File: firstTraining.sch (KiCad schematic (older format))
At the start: 5 parts

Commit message: 配線した
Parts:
- added C?: CP1, symbol Device:CP1
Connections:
- net AC: now reaches T?.1 (AA)
- net GND: now reaches T?.2 (AB)
- net GND: now also C?.2, C?.2, T?.4 (SC), U?.2 (GND), C?.2
- net at T?.3 (SA): now also D?.4 (~~)
- net at T?.5 (SB): now also D?.3 (~~)
- net at D?.1 (+): now also C?.1, U?.1 (IN)
- net at D?.2 (-): now also C?.1
- net at U?.3 (OUT): now also C?.1
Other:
- moved on the sheet: C?, D?, T?, U?
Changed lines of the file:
@@
 EESchema Schematic File Version 4
+LIBS:firstTraining-cache
 EELAYER 26 0
 EELAYER END
@@
 L Device:Transformer_1P_SS T?
 U 1 1 5BD5E741
-P 3900 2550
-F 0 "T?" H 3900 2928 50  0000 C CNN
-F 1 "Transformer_1P_SS" H 3900 2837 50  0000 C CNN
-F 2 "" H 3900 2550 50  0001 C CNN
-F 3 "~" H 3900 2550 50  0001 C CNN
-	1    3900 2550
+P 1700 1500
+F 0 "T?" H 1700 1878 50  0000 C CNN
+F 1 "Transformer_1P_SS" H 1700 1787 50  0000 C CNN
+F 2 "" H 1700 1500 50  0001 C CNN
+F 3 "~" H 1700 1500 50  0001 C CNN
+	1    1700 1500
 	1    0    0    -1
 $EndComp
@@
 L Device:D_Bridge_+-AA D?
 U 1 1 5BD5E940
-P 5000 2550
-F 0 "D?" H 5341 2596 50  0000 L CNN
-F 1 "D_Bridge_+-AA" H 5341 2505 50  0000 L CNN
-F 2 "" H 5000 2550 50  0001 C CNN
-F 3 "~" H 5000 2550 50  0001 C CNN
-	1    5000 2550
+P 2800 1500
+F 0 "D?" H 3141 1546 50  0000 L CNN
+F 1 "D_Bridge_+-AA" H 3141 1455 50  0000 L CNN
+F 2 "" H 2800 1500 50  0001 C CNN
+F 3 "~" H 2800 1500 50  0001 C CNN
+	1    2800 1500
 	1    0    0    -1
 $EndComp
@@
 L Device:CP1 C?
 U 1 1 5BD5EB54
-P 6300 2550
-F 0 "C?" H 6415 2596 50  0000 L CNN
-F 1 "CP1" H 6415 2505 50  0000 L CNN
-F 2 "" H 6300 2550 50  0001 C CNN
-F 3 "~" H 6300 2550 50  0001 C CNN
-	1    6300 2550
+P 4100 1500
+F 0 "C?" H 4215 1546 50  0000 L CNN
+F 1 "CP1" H 4215 1455 50  0000 L CNN
+F 2 "" H 4100 1500 50  0001 C CNN
+F 3 "~" H 4100 1500 50  0001 C CNN
+	1    4100 1500
 	1    0    0    -1
 $EndComp
@@
 L Regulator_Linear:L7805 U?
 U 1 1 5BD5FA9A
-P 7200 2500
-F 0 "U?" H 7200 2742 50  0000 C CNN
-F 1 "L7805" H 7200 2651 50  0000 C CNN
-F 2 "" H 7225 2350 50  0001 L CIN
-F 3 "http://www.st.com/content/ccc/resource/technical/document/datasheet/41/4f/b3/b0/12/d4/47/88/CD00000444.pdf/files/CD00000444.pdf/jcr:content/translations/en.CD00000444.pdf" H 7200 2450 50  0001 C CNN
-	1    7200 2500
+P 5000 1450
+F 0 "U?" H 5000 1692 50  0000 C CNN
+F 1 "L7805" H 5000 1601 50  0000 C CNN
+F 2 "" H 5025 1300 50  0001 L CIN
+F 3 "http://www.st.com/content/ccc/resource/technical/document/datasheet/41/4f/b3/b0/12/d4/47/88/CD00000444.pdf/files/CD00000444.pdf/jcr:content/translations/en.CD00000444.pdf" H 5000 1400 50  0001 C CNN
+	1    5000 1450
 	1    0    0    -1
 $EndComp
@@
 L Device:C C?
 U 1 1 5BD5FBB0
-P 7900 2600
-F 0 "C?" H 8015 2646 50  0000 L CNN
-F 1 "C" H 8015 2555 50  0000 L CNN
-F 2 "" H 7938 2450 50  0001 C CNN
-F 3 "~" H 7900 2600 50  0001 C CNN
-	1    7900 2600
+P 5700 1550
+F 0 "C?" H 5815 1596 50  0000 L CNN
+F 1 "C" H 5815 1505 50  0000 L CNN
+F 2 "" H 5738 1400 50  0001 C CNN
+F 3 "~" H 5700 1550 50  0001 C CNN
+	1    5700 1550
 	1    0    0    -1
 $EndComp
+$Comp
+L power:AC #PWR?
+U 1 1 5BD65D78
+P 1050 1300
+F 0 "#PWR?" H 1050 1200 50  0001 C CNN
+F 1 "AC" H 1050 1575 50  0000 C CNN
+F 2 "" H 1050 1300 50  0001 C CNN
+F 3 "" H 1050 1300 50  0001 C CNN
+	1    1050 1300
+	1    0    0    -1
+$EndComp
+Wire Wire Line
+	2100 1300 2350 1300
+Wire Wire Line
+	2350 1300 2350 1200
+Wire Wire Line
+	2350 1200 2800 1200
+Wire Wire Line
+	2400 1700 2400 1800
+Wire Wire Line
+	2400 1800 2800 1800
+Wire Wire Line
+	2100 1700 2400 1700
+Wire Wire Line
+	1050 1300 1300 1300
+$Comp
+L power:GND #PWR?
+U 1 1 5BD65E35
+P 1000 1700
+F 0 "#PWR?" H 1000 1450 50  0001 C CNN
+F 1 "GND" H 1005 1527 50  0000 C CNN
+F 2 "" H 1000 1700 50  0001 C CNN
+F 3 "" H 1000 1700 50  0001 C CNN
+	1    1000 1700
+	1    0    0    -1
+$EndComp
+Wire Wire Line
+	1300 1700 1000 1700
+Wire Wire Line
+	4100 1900 4100 1650
+Wire Wire Line
+	3100 1500 3100 1350
+Wire Wire Line
+	3100 1350 4100 1350
+Wire Wire Line
+	2100 1500 2250 1500
+Wire Wire Line
+	2250 1500 2250 1900
+Wire Wire Line
+	2250 1900 3300 1900
+Wire Wire Line
+	4100 1350 4700 1350
+Wire Wire Line
+	4700 1350 4700 1450
+Connection ~ 4100 1350
+Wire Wire Line
+	5300 1450 5500 1450
+Wire Wire Line
+	5500 1450 5500 1400
+Wire Wire Line
+	5500 1400 5700 1400
+$Comp
+L power:GND #PWR?
+U 1 1 5BD66352
+P 5000 1750
+F 0 "#PWR?" H 5000 1500 50  0001 C CNN
+F 1 "GND" H 5005 1577 50  0000 C CNN
+F 2 "" H 5000 1750 50  0001 C CNN
+F 3 "" H 5000 1750 50  0001 C CNN
+	1    5000 1750
+	1    0    0    -1
+$EndComp
+$Comp
+L power:GND #PWR?
+U 1 1 5BD6637E
+P 5700 1700
+F 0 "#PWR?" H 5700 1450 50  0001 C CNN
+F 1 "GND" H 5705 1527 50  0000 C CNN
+F 2 "" H 5700 1700 50  0001 C CNN
+F 3 "" H 5700 1700 50  0001 C CNN
+	1    5700 1700
+	1    0    0    -1
+$EndComp
+$Comp
+L power:GND #PWR?
+U 1 1 5BD663AA
+P 3300 1900
+F 0 "#PWR?" H 3300 1650 50  0001 C CNN
+F 1 "GND" H 3305 1727 50  0000 C CNN
+F 2 "" H 3300 1900 50  0001 C CNN
+F 3 "" H 3300 1900 50  0001 C CNN
+	1    3300 1900
+	1    0    0    -1
+$EndComp
+Connection ~ 3300 1900
+Wire Wire Line
+	3300 1900 4100 1900
+$Comp
+L Device:CP1 C?
+U 1 1 5BD667AC
+P 4100 2050
+F 0 "C?" H 3985 2004 50  0000 R CNN
+F 1 "CP1" H 3985 2095 50  0000 R CNN
+F 2 "" H 4100 2050 50  0001 C CNN
+F 3 "~" H 4100 2050 50  0001 C CNN
+	1    4100 2050
+	1    0    0    1
+$EndComp
+Connection ~ 4100 1900
+Wire Wire Line
+	2500 1500 2500 2200
+Wire Wire Line
+	2500 2200 4100 2200
 $EndSCHEMATC

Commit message: 部品の場所を再配置
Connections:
- wire segments 22 -> 19
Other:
- moved on the sheet: C?, U?
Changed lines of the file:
@@
 L Device:CP1 C?
 U 1 1 5BD5EB54
-P 4100 1500
-F 0 "C?" H 4215 1546 50  0000 L CNN
-F 1 "CP1" H 4215 1455 50  0000 L CNN
-F 2 "" H 4100 1500 50  0001 C CNN
-F 3 "~" H 4100 1500 50  0001 C CNN
-	1    4100 1500
+P 4100 1650
+F 0 "C?" H 4215 1696 50  0000 L CNN
+F 1 "CP1" H 4215 1605 50  0000 L CNN
+F 2 "" H 4100 1650 50  0001 C CNN
+F 3 "~" H 4100 1650 50  0001 C CNN
+	1    4100 1650
 	1    0    0    -1
 $EndComp
@@
 L Regulator_Linear:L7805 U?
 U 1 1 5BD5FA9A
-P 5000 1450
-F 0 "U?" H 5000 1692 50  0000 C CNN
-F 1 "L7805" H 5000 1601 50  0000 C CNN
-F 2 "" H 5025 1300 50  0001 L CIN
-F 3 "http://www.st.com/content/ccc/resource/technical/document/datasheet/41/4f/b3/b0/12/d4/47/88/CD00000444.pdf/files/CD00000444.pdf/jcr:content/translations/en.CD00000444.pdf" H 5000 1400 50  0001 C CNN
-	1    5000 1450
+P 5000 1500
+F 0 "U?" H 5000 1742 50  0000 C CNN
+F 1 "L7805" H 5000 1651 50  0000 C CNN
+F 2 "" H 5025 1350 50  0001 L CIN
+F 3 "http://www.st.com/content/ccc/resource/technical/document/datasheet/41/4f/b3/b0/12/d4/47/88/CD00000444.pdf/files/CD00000444.pdf/jcr:content/translations/en.CD00000444.pdf" H 5000 1450 50  0001 C CNN
+	1    5000 1500
 	1    0    0    -1
 $EndComp
@@
 L Device:C C?
 U 1 1 5BD5FBB0
-P 5700 1550
-F 0 "C?" H 5815 1596 50  0000 L CNN
-F 1 "C" H 5815 1505 50  0000 L CNN
-F 2 "" H 5738 1400 50  0001 C CNN
-F 3 "~" H 5700 1550 50  0001 C CNN
-	1    5700 1550
+P 5700 1650
+F 0 "C?" H 5815 1696 50  0000 L CNN
+F 1 "C" H 5815 1605 50  0000 L CNN
+F 2 "" H 5738 1500 50  0001 C CNN
+F 3 "~" H 5700 1650 50  0001 C CNN
+	1    5700 1650
 	1    0    0    -1
 $EndComp
@@
 	1300 1700 1000 1700
 Wire Wire Line
-	4100 1900 4100 1650
+	4100 2050 4100 1800
 Wire Wire Line
 	3100 1500 3100 1350
 Wire Wire Line
-	3100 1350 4100 1350
+	3100 1500 4100 1500
 Wire Wire Line
 	2100 1500 2250 1500
 Wire Wire Line
-	2250 1500 2250 1900
+	2250 2050 3300 2050
 Wire Wire Line
-	2250 1900 3300 1900
-Wire Wire Line
-	4100 1350 4700 1350
-Wire Wire Line
-	4700 1350 4700 1450
-Connection ~ 4100 1350
-Wire Wire Line
-	5300 1450 5500 1450
-Wire Wire Line
-	5500 1450 5500 1400
-Wire Wire Line
-	5500 1400 5700 1400
+	4100 1500 4700 1500
+Connection ~ 4100 1500
 $Comp
 L power:GND #PWR?
 U 1 1 5BD66352
-P 5000 1750
-F 0 "#PWR?" H 5000 1500 50  0001 C CNN
-F 1 "GND" H 5005 1577 50  0000 C CNN
-F 2 "" H 5000 1750 50  0001 C CNN
-F 3 "" H 5000 1750 50  0001 C CNN
-	1    5000 1750
+P 5000 1900
+F 0 "#PWR?" H 5000 1650 50  0001 C CNN
+F 1 "GND" H 5005 1727 50  0000 C CNN
+F 2 "" H 5000 1900 50  0001 C CNN
+F 3 "" H 5000 1900 50  0001 C CNN
+	1    5000 1900
 	1    0    0    -1
 $EndComp
@@
 L power:GND #PWR?
 U 1 1 5BD6637E
-P 5700 1700
-F 0 "#PWR?" H 5700 1450 50  0001 C CNN
-F 1 "GND" H 5705 1527 50  0000 C CNN
-F 2 "" H 5700 1700 50  0001 C CNN
-F 3 "" H 5700 1700 50  0001 C CNN
-	1    5700 1700
+P 5700 1800
+F 0 "#PWR?" H 5700 1550 50  0001 C CNN
+F 1 "GND" H 5705 1627 50  0000 C CNN
+F 2 "" H 5700 1800 50  0001 C CNN
+F 3 "" H 5700 1800 50  0001 C CNN
+	1    5700 1800
 	1    0    0    -1
 $EndComp
@@
 L power:GND #PWR?
 U 1 1 5BD663AA
-P 3300 1900
-F 0 "#PWR?" H 3300 1650 50  0001 C CNN
-F 1 "GND" H 3305 1727 50  0000 C CNN
-F 2 "" H 3300 1900 50  0001 C CNN
-F 3 "" H 3300 1900 50  0001 C CNN
-	1    3300 1900
+P 3300 2050
+F 0 "#PWR?" H 3300 1800 50  0001 C CNN
+F 1 "GND" H 3305 1877 50  0000 C CNN
+F 2 "" H 3300 2050 50  0001 C CNN
+F 3 "" H 3300 2050 50  0001 C CNN
+	1    3300 2050
 	1    0    0    -1
 $EndComp
-Connection ~ 3300 1900
+Connection ~ 3300 2050
 Wire Wire Line
-	3300 1900 4100 1900
+	3300 2050 4100 2050
 $Comp
 L Device:CP1 C?
 U 1 1 5BD667AC
-P 4100 2050
-F 0 "C?" H 3985 2004 50  0000 R CNN
-F 1 "CP1" H 3985 2095 50  0000 R CNN
-F 2 "" H 4100 2050 50  0001 C CNN
-F 3 "~" H 4100 2050 50  0001 C CNN
-	1    4100 2050
-	1    0    0    1
+P 4100 2200
+F 0 "C?" H 3985 2154 50  0000 R CNN
+F 1 "CP1" H 3985 2245 50  0000 R CNN
+F 2 "" H 4100 2200 50  0001 C CNN
+F 3 "~" H 4100 2200 50  0001 C CNN
+	1    4100 2200
+	-1   0    0    -1
 $EndComp
-Connection ~ 4100 1900
+Connection ~ 4100 2050
 Wire Wire Line
-	2500 1500 2500 2200
+	2500 2350 4100 2350
 Wire Wire Line
-	2500 2200 4100 2200
+	5300 1500 5700 1500
+Connection ~ 3100 1500
+Wire Wire Line
+	2250 1500 2250 2050
+Wire Wire Line
+	2500 1500 2500 2350
 $EndSCHEMATC

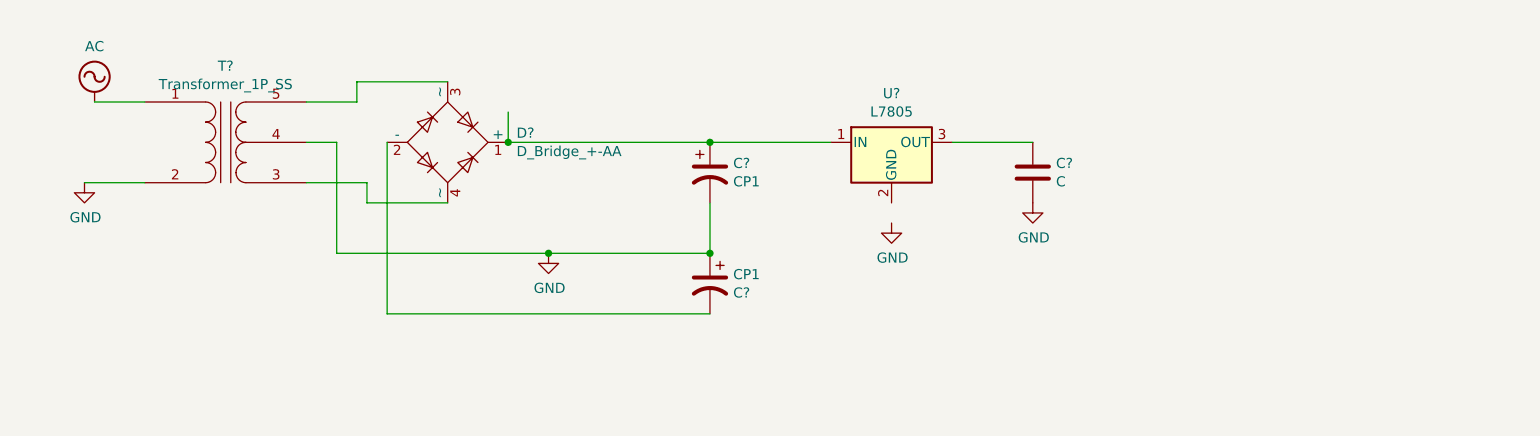
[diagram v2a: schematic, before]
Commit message: 3V3電源を追加
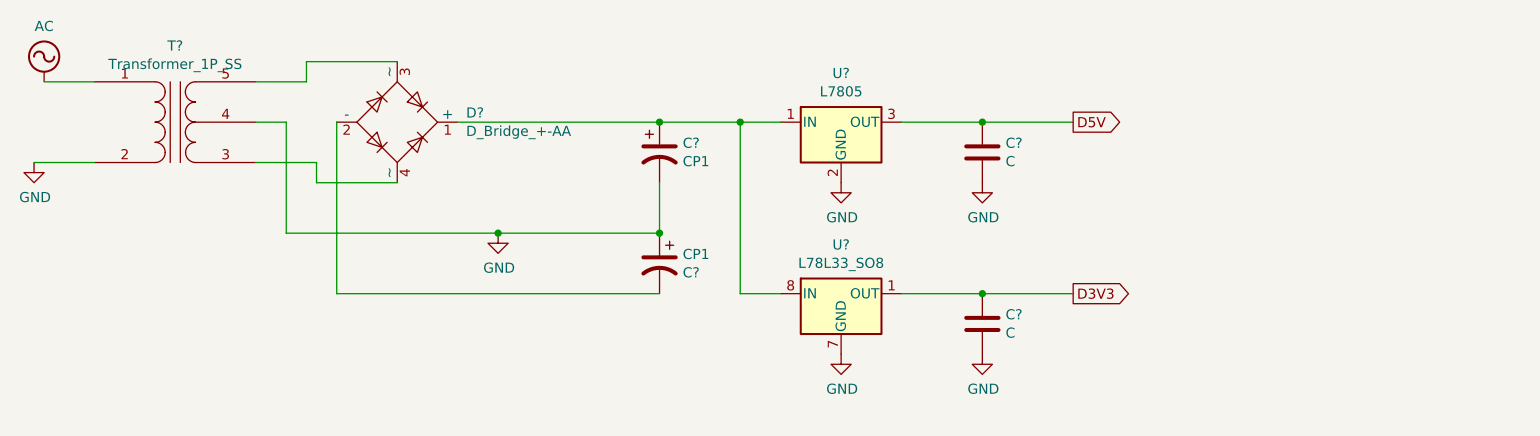
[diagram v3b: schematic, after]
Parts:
- added C?: C, symbol Device:C
- added U?: L78L33_SO8, Package_SO:SOIC-8_3.9x4.9mm_P1.27mm, symbol Regulator_Linear:L78L33_SO8
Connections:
- net labels added: D3V3, D5V
- wire segments 19 -> 24
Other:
- moved on the sheet: C?, D?, T?, U?
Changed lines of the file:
@@
 L Device:Transformer_1P_SS T?
 U 1 1 5BD5E741
-P 1700 1500
-F 0 "T?" H 1700 1878 50  0000 C CNN
-F 1 "Transformer_1P_SS" H 1700 1787 50  0000 C CNN
-F 2 "" H 1700 1500 50  0001 C CNN
-F 3 "~" H 1700 1500 50  0001 C CNN
-	1    1700 1500
+P 1450 1400
+F 0 "T?" H 1450 1778 50  0000 C CNN
+F 1 "Transformer_1P_SS" H 1450 1687 50  0000 C CNN
+F 2 "" H 1450 1400 50  0001 C CNN
+F 3 "~" H 1450 1400 50  0001 C CNN
+	1    1450 1400
 	1    0    0    -1
 $EndComp
@@
 L Device:D_Bridge_+-AA D?
 U 1 1 5BD5E940
-P 2800 1500
-F 0 "D?" H 3141 1546 50  0000 L CNN
-F 1 "D_Bridge_+-AA" H 3141 1455 50  0000 L CNN
-F 2 "" H 2800 1500 50  0001 C CNN
-F 3 "~" H 2800 1500 50  0001 C CNN
-	1    2800 1500
+P 2550 1400
+F 0 "D?" H 2891 1446 50  0000 L CNN
+F 1 "D_Bridge_+-AA" H 2891 1355 50  0000 L CNN
+F 2 "" H 2550 1400 50  0001 C CNN
+F 3 "~" H 2550 1400 50  0001 C CNN
+	1    2550 1400
 	1    0    0    -1
 $EndComp
@@
 L Device:CP1 C?
 U 1 1 5BD5EB54
-P 4100 1650
-F 0 "C?" H 4215 1696 50  0000 L CNN
-F 1 "CP1" H 4215 1605 50  0000 L CNN
-F 2 "" H 4100 1650 50  0001 C CNN
-F 3 "~" H 4100 1650 50  0001 C CNN
-	1    4100 1650
+P 3850 1550
+F 0 "C?" H 3965 1596 50  0000 L CNN
+F 1 "CP1" H 3965 1505 50  0000 L CNN
+F 2 "" H 3850 1550 50  0001 C CNN
+F 3 "~" H 3850 1550 50  0001 C CNN
+	1    3850 1550
 	1    0    0    -1
 $EndComp
@@
 L Regulator_Linear:L7805 U?
 U 1 1 5BD5FA9A
-P 5000 1500
-F 0 "U?" H 5000 1742 50  0000 C CNN
-F 1 "L7805" H 5000 1651 50  0000 C CNN
-F 2 "" H 5025 1350 50  0001 L CIN
-F 3 "http://www.st.com/content/ccc/resource/technical/document/datasheet/41/4f/b3/b0/12/d4/47/88/CD00000444.pdf/files/CD00000444.pdf/jcr:content/translations/en.CD00000444.pdf" H 5000 1450 50  0001 C CNN
-	1    5000 1500
+P 4750 1400
+F 0 "U?" H 4750 1642 50  0000 C CNN
+F 1 "L7805" H 4750 1551 50  0000 C CNN
+F 2 "" H 4775 1250 50  0001 L CIN
+F 3 "http://www.st.com/content/ccc/resource/technical/document/datasheet/41/4f/b3/b0/12/d4/47/88/CD00000444.pdf/files/CD00000444.pdf/jcr:content/translations/en.CD00000444.pdf" H 4750 1350 50  0001 C CNN
+	1    4750 1400
 	1    0    0    -1
 $EndComp
@@
 L Device:C C?
 U 1 1 5BD5FBB0
-P 5700 1650
-F 0 "C?" H 5815 1696 50  0000 L CNN
-F 1 "C" H 5815 1605 50  0000 L CNN
-F 2 "" H 5738 1500 50  0001 C CNN
-F 3 "~" H 5700 1650 50  0001 C CNN
-	1    5700 1650
+P 5450 1550
+F 0 "C?" H 5565 1596 50  0000 L CNN
+F 1 "C" H 5565 1505 50  0000 L CNN
+F 2 "" H 5488 1400 50  0001 C CNN
+F 3 "~" H 5450 1550 50  0001 C CNN
+	1    5450 1550
 	1    0    0    -1
 $EndComp
@@
 L power:AC #PWR?
 U 1 1 5BD65D78
-P 1050 1300
-F 0 "#PWR?" H 1050 1200 50  0001 C CNN
-F 1 "AC" H 1050 1575 50  0000 C CNN
-F 2 "" H 1050 1300 50  0001 C CNN
-F 3 "" H 1050 1300 50  0001 C CNN
-	1    1050 1300
-	1    0    0    -1
-$EndComp
-Wire Wire Line
-	2100 1300 2350 1300
-Wire Wire Line
-	2350 1300 2350 1200
-Wire Wire Line
-	2350 1200 2800 1200
-Wire Wire Line
-	2400 1700 2400 1800
-Wire Wire Line
-	2400 1800 2800 1800
-Wire Wire Line
-	2100 1700 2400 1700
-Wire Wire Line
-	1050 1300 1300 1300
+P 800 1200
+F 0 "#PWR?" H 800 1100 50  0001 C CNN
+F 1 "AC" H 800 1475 50  0000 C CNN
+F 2 "" H 800 1200 50  0001 C CNN
+F 3 "" H 800 1200 50  0001 C CNN
+	1    800  1200
+	1    0    0    -1
+$EndComp
+Wire Wire Line
+	1850 1200 2100 1200
+Wire Wire Line
+	2100 1200 2100 1100
+Wire Wire Line
+	2100 1100 2550 1100
+Wire Wire Line
+	2150 1600 2150 1700
+Wire Wire Line
+	2150 1700 2550 1700
+Wire Wire Line
+	1850 1600 2150 1600
+Wire Wire Line
+	800  1200 1050 1200
 $Comp
 L power:GND #PWR?
 U 1 1 5BD65E35
-P 1000 1700
-F 0 "#PWR?" H 1000 1450 50  0001 C CNN
-F 1 "GND" H 1005 1527 50  0000 C CNN
-F 2 "" H 1000 1700 50  0001 C CNN
-F 3 "" H 1000 1700 50  0001 C CNN
-	1    1000 1700
-	1    0    0    -1
-$EndComp
-Wire Wire Line
-	1300 1700 1000 1700
-Wire Wire Line
-	4100 2050 4100 1800
-Wire Wire Line
-	3100 1500 3100 1350
-Wire Wire Line
-	3100 1500 4100 1500
-Wire Wire Line
-	2100 1500 2250 1500
-Wire Wire Line
-	2250 2050 3300 2050
-Wire Wire Line
-	4100 1500 4700 1500
-Connection ~ 4100 1500
+P 750 1600
+F 0 "#PWR?" H 750 1350 50  0001 C CNN
+F 1 "GND" H 755 1427 50  0000 C CNN
+F 2 "" H 750 1600 50  0001 C CNN
+F 3 "" H 750 1600 50  0001 C CNN
+	1    750  1600
+	1    0    0    -1
+$EndComp
+Wire Wire Line
+	1050 1600 750  1600
+Wire Wire Line
+	3850 1950 3850 1700
+Wire Wire Line
+	2850 1400 3850 1400
+Wire Wire Line
+	1850 1400 2000 1400
+Wire Wire Line
+	2000 1950 3050 1950
+Wire Wire Line
+	3850 1400 4250 1400
+Connection ~ 3850 1400
 $Comp
 L power:GND #PWR?
 U 1 1 5BD66352
-P 5000 1900
-F 0 "#PWR?" H 5000 1650 50  0001 C CNN
-F 1 "GND" H 5005 1727 50  0000 C CNN
-F 2 "" H 5000 1900 50  0001 C CNN
-F 3 "" H 5000 1900 50  0001 C CNN
-	1    5000 1900
+P 4750 1700
+F 0 "#PWR?" H 4750 1450 50  0001 C CNN
+F 1 "GND" H 4755 1527 50  0000 C CNN
+F 2 "" H 4750 1700 50  0001 C CNN
+F 3 "" H 4750 1700 50  0001 C CNN
+	1    4750 1700
 	1    0    0    -1
 $EndComp
@@
 L power:GND #PWR?
 U 1 1 5BD6637E
-P 5700 1800
-F 0 "#PWR?" H 5700 1550 50  0001 C CNN
-F 1 "GND" H 5705 1627 50  0000 C CNN
-F 2 "" H 5700 1800 50  0001 C CNN
-F 3 "" H 5700 1800 50  0001 C CNN
-	1    5700 1800
+P 5450 1700
+F 0 "#PWR?" H 5450 1450 50  0001 C CNN
+F 1 "GND" H 5455 1527 50  0000 C CNN
+F 2 "" H 5450 1700 50  0001 C CNN
+F 3 "" H 5450 1700 50  0001 C CNN
+	1    5450 1700
 	1    0    0    -1
 $EndComp
@@
 L power:GND #PWR?
 U 1 1 5BD663AA
-P 3300 2050
-F 0 "#PWR?" H 3300 1800 50  0001 C CNN
-F 1 "GND" H 3305 1877 50  0000 C CNN
-F 2 "" H 3300 2050 50  0001 C CNN
-F 3 "" H 3300 2050 50  0001 C CNN
-	1    3300 2050
-	1    0    0    -1
-$EndComp
-Connection ~ 3300 2050
-Wire Wire Line
-	3300 2050 4100 2050
+P 3050 1950
+F 0 "#PWR?" H 3050 1700 50  0001 C CNN
+F 1 "GND" H 3055 1777 50  0000 C CNN
+F 2 "" H 3050 1950 50  0001 C CNN
+F 3 "" H 3050 1950 50  0001 C CNN
+	1    3050 1950
+	1    0    0    -1
+$EndComp
+Connection ~ 3050 1950
+Wire Wire Line
+	3050 1950 3850 1950
 $Comp
 L Device:CP1 C?
 U 1 1 5BD667AC
-P 4100 2200
-F 0 "C?" H 3985 2154 50  0000 R CNN
-F 1 "CP1" H 3985 2245 50  0000 R CNN
-F 2 "" H 4100 2200 50  0001 C CNN
-F 3 "~" H 4100 2200 50  0001 C CNN
-	1    4100 2200
+P 3850 2100
+F 0 "C?" H 3735 2054 50  0000 R CNN
+F 1 "CP1" H 3735 2145 50  0000 R CNN
+F 2 "" H 3850 2100 50  0001 C CNN
+F 3 "~" H 3850 2100 50  0001 C CNN
+	1    3850 2100
 	-1   0    0    -1
 $EndComp
-Connection ~ 4100 2050
-Wire Wire Line
-	2500 2350 4100 2350
-Wire Wire Line
-	5300 1500 5700 1500
-Connection ~ 3100 1500
-Wire Wire Line
-	2250 1500 2250 2050
-Wire Wire Line
-	2500 1500 2500 2350
+Connection ~ 3850 1950
+Wire Wire Line
+	2250 2250 3850 2250
+Wire Wire Line
+	5050 1400 5450 1400
+Wire Wire Line
+	2000 1400 2000 1950
+Wire Wire Line
+	2250 1400 2250 2250
+$Comp
+L Regulator_Linear:L78L33_SO8 U?
+U 1 1 5BD704B9
+P 4750 2250
+F 0 "U?" H 4750 2492 50  0000 C CNN
+F 1 "L78L33_SO8" H 4750 2401 50  0000 C CNN
+F 2 "Package_SO:SOIC-8_3.9x4.9mm_P1.27mm" H 4850 2450 50  0001 C CIN
+F 3 "http://www.st.com/content/ccc/resource/technical/document/datasheet/15/55/e5/aa/23/5b/43/fd/CD00000446.pdf/files/CD00000446.pdf/jcr:content/translations/en.CD00000446.pdf" H 4950 2250 50  0001 C CNN
+	1    4750 2250
+	1    0    0    -1
+$EndComp
+Wire Wire Line
+	4250 1400 4250 2250
+Wire Wire Line
+	4250 2250 4450 2250
+Connection ~ 4250 1400
+Wire Wire Line
+	4250 1400 4450 1400
+$Comp
+L Device:C C?
+U 1 1 5BD706DF
+P 5450 2400
+F 0 "C?" H 5565 2446 50  0000 L CNN
+F 1 "C" H 5565 2355 50  0000 L CNN
+F 2 "" H 5488 2250 50  0001 C CNN
+F 3 "~" H 5450 2400 50  0001 C CNN
+	1    5450 2400
+	1    0    0    -1
+$EndComp
+Wire Wire Line
+	5050 2250 5450 2250
+$Comp
+L power:GND #PWR?
+U 1 1 5BD70953
+P 5450 2550
+F 0 "#PWR?" H 5450 2300 50  0001 C CNN
+F 1 "GND" H 5455 2377 50  0000 C CNN
+F 2 "" H 5450 2550 50  0001 C CNN
+F 3 "" H 5450 2550 50  0001 C CNN
+	1    5450 2550
+	1    0    0    -1
+$EndComp
+$Comp
+L power:GND #PWR?
+U 1 1 5BD70985
+P 4750 2550
+F 0 "#PWR?" H 4750 2300 50  0001 C CNN
+F 1 "GND" H 4755 2377 50  0000 C CNN
+F 2 "" H 4750 2550 50  0001 C CNN
+F 3 "" H 4750 2550 50  0001 C CNN
+	1    4750 2550
+	1    0    0    -1
+$EndComp
+Text GLabel 5900 1400 2    50   Output ~ 0
+D5V
+Wire Wire Line
+	5450 1400 5900 1400
+Connection ~ 5450 1400
+Text GLabel 5900 2250 2    50   Output ~ 0
+D3V3
+Wire Wire Line
+	5450 2250 5900 2250
+Connection ~ 5450 2250
 $EndSCHEMATC

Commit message: アノテーションとERC実行
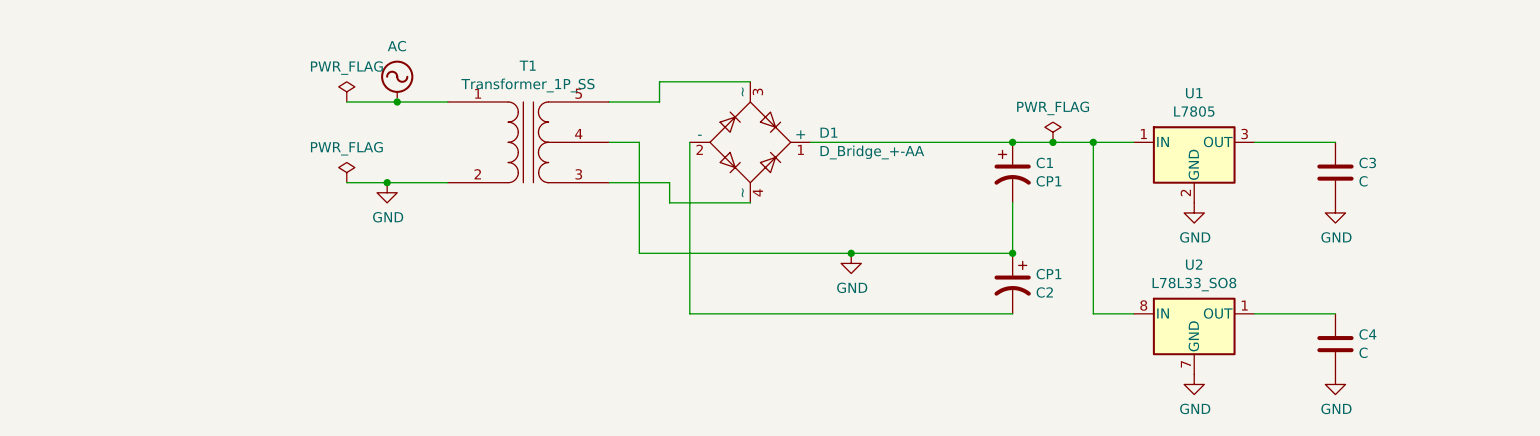
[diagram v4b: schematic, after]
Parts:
- gave numbers to parts that had none: 8
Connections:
- net D3V3: no longer names the net of C4.1, U2.1 (OUT)
- net D5V: no longer names the net of C3.1, U1.3 (OUT)
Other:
- moved on the sheet: C1, C2, C3, C4, D1, T1, U1, U2
